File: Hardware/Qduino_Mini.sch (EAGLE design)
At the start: 39 parts, among them Q1 PFET, U1 ATMEGA32U4QFN, U2 MCP73831, U3 MAX17048, U4 TPS78233, Y1 16MHz

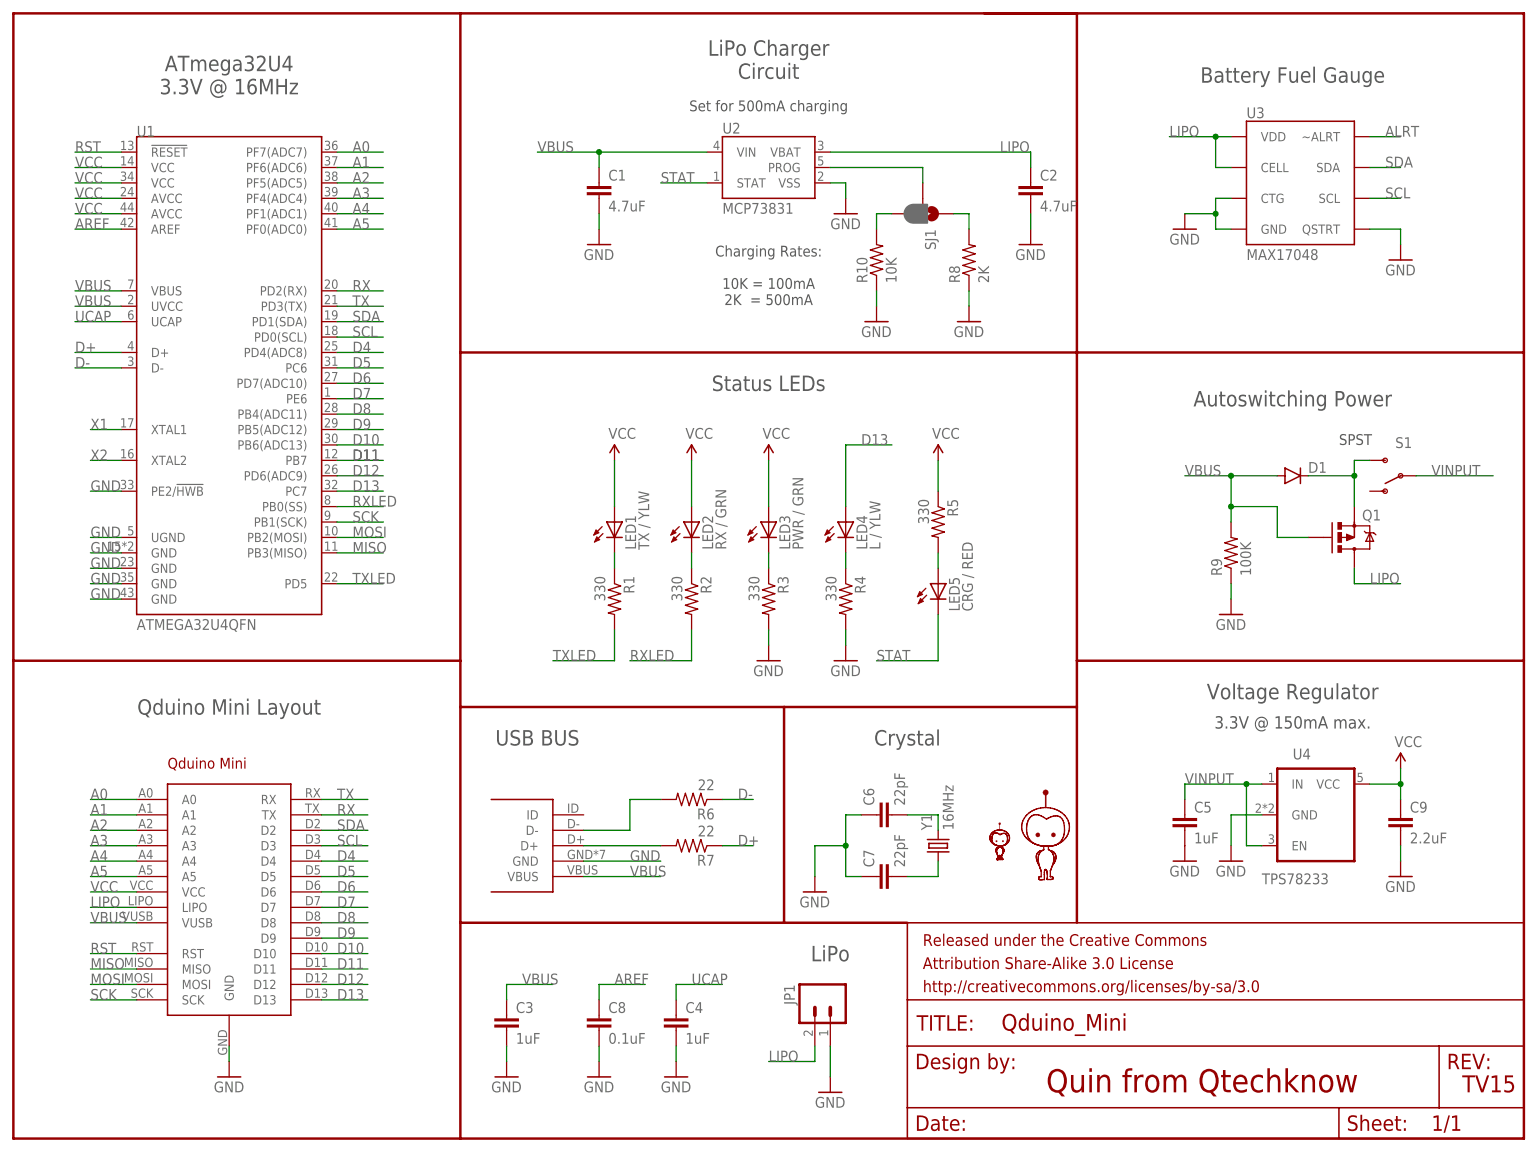
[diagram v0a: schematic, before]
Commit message: Converted simple things to SparkFun styles
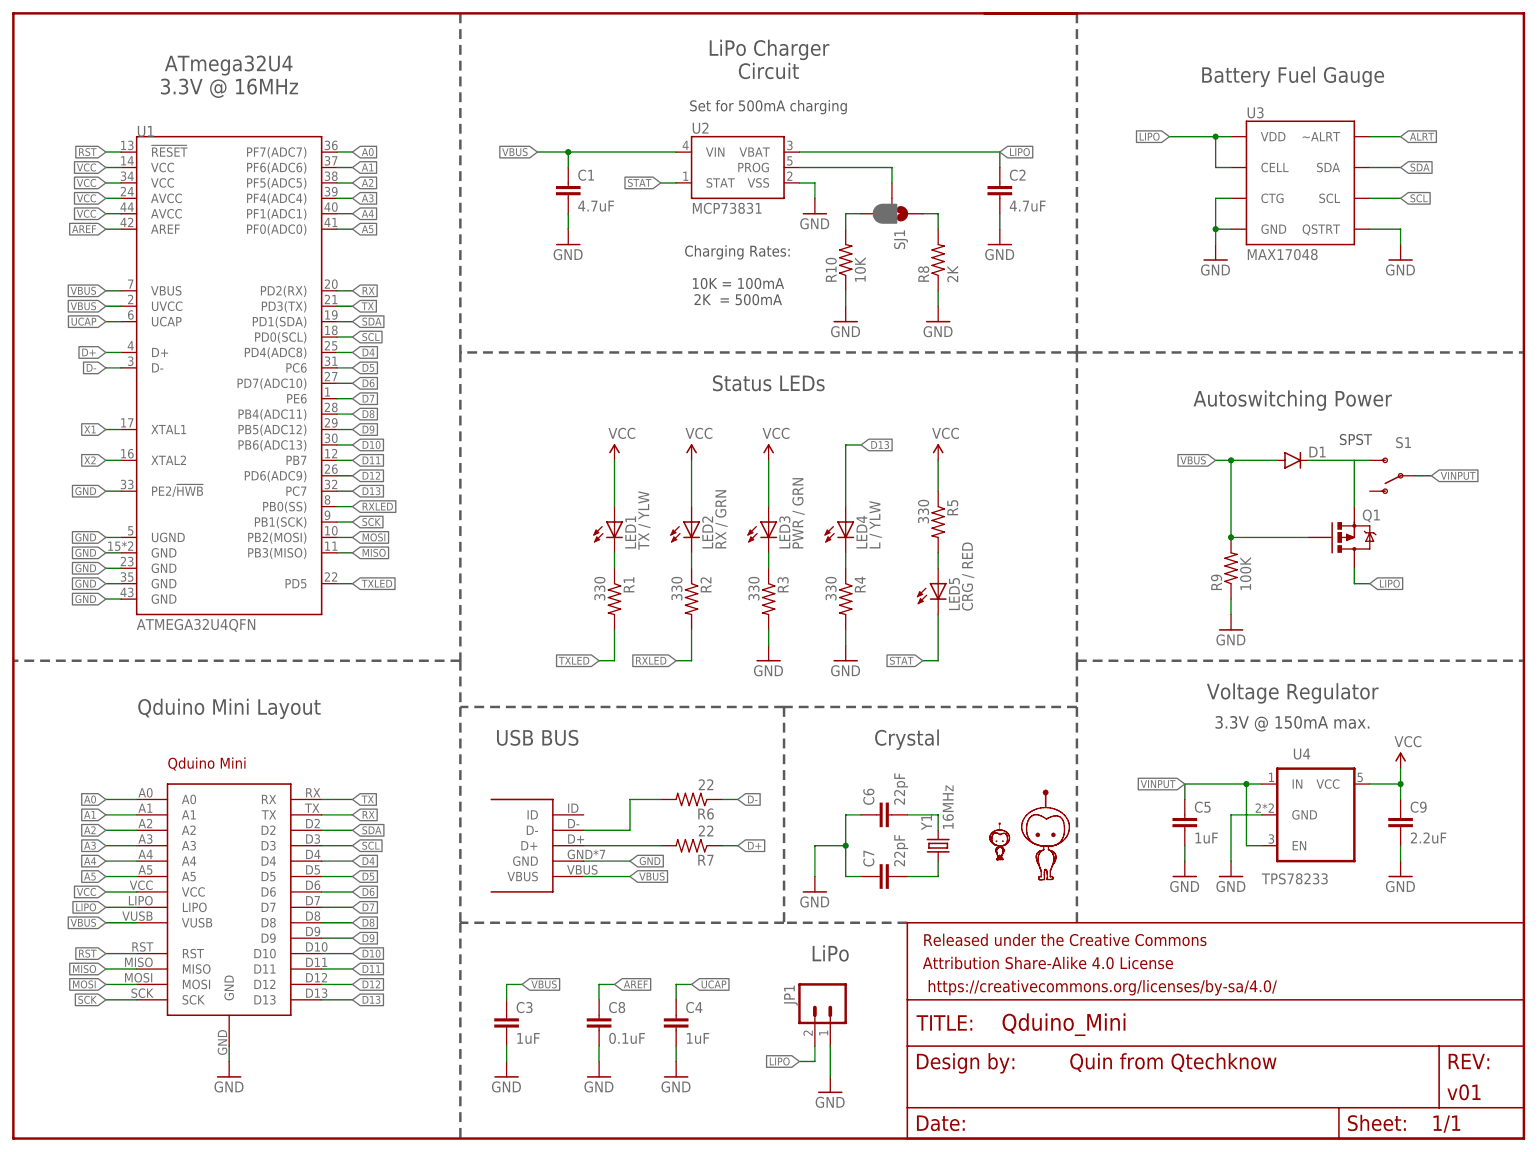
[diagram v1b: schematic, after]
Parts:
- FRAME2: value FRAME-LETTER -> (none); DESIGNER (none) -> Quin from Qtechknow
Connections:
- new net N$3: Q1.S
- net INMOSFET: no longer Q1.S
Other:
- note removed: "Quin from Qtechknow"
- note removed: "TV15"
- moved on the sheet: C1, C2, D1, R10, R8, R9, SJ1, U2

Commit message: Added pullup resistors, added alrt interrupt trace, added PROD_ID to each part, swapped out SFE already used parts, etc
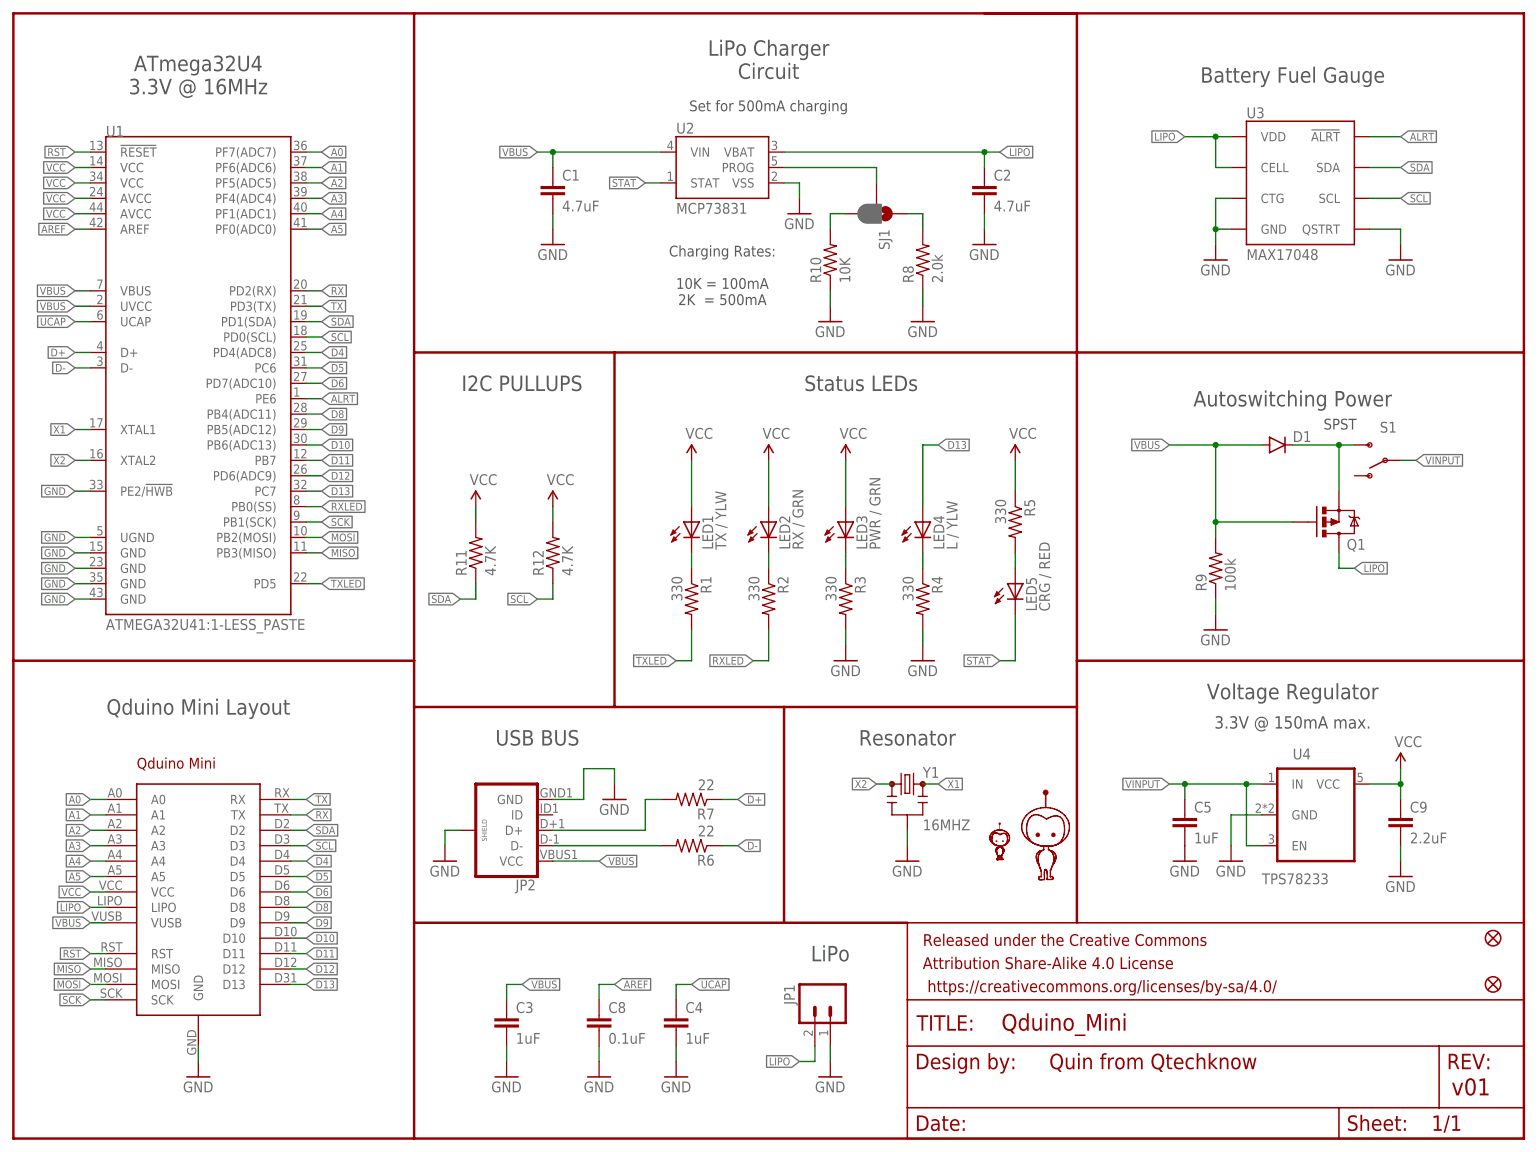
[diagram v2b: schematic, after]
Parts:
- removed C6, C7: 22pF, SparkFun-Passives:CAP0603-CAP
- removed JP3: QDUINOMINI, Qtechknow:QDUINOMINI
- added FID5, FID6: FIDUCIAL1X2, SparkFun-Aesthetics:FIDUCIAL1X2
- added R11, R12: 4.7K, SparkFun-Passives:RESISTOR0603-RES
- added U7: DNP, Qtechknow:QDUINOMINI
- C1, C2: PROD_ID (none) -> CAP-10300
- C3, C4, C5: PROD_ID (none) -> CAP-00868
- C8: device SparkFun-Passives:CAP0603-CAP -> SparkFun-Capacitors:0.1UF-25V(+80/-20%)(0603)
- C9: device SparkFun-Passives:CAP0603-CAP -> SparkFun-Capacitors:2.2UF-10V-20%(0603)
- FRAME2: DESIGNER Quin from Qtechknow -> (none)
- JP1: PROD_ID (none) -> CONN-11443
- JP2: value USB-MICROBQ -> USB_MICROB_PLUGCONN-11752; device SFE-Sockets:USB-MICROBQ -> SparkFun-Connectors:USB_MICROB_PLUGCONN-11752
- LED1, LED4: PROD_ID (none) -> DIO-09003
- LED2, LED3: PROD_ID (none) -> DIO-00821
- LED5: PROD_ID (none) -> DIO-00819
- Q1: device Pinoccio:MOSFET-PCHANNELSMD -> SparkFun-DiscreteSemi:MOSFET-PCHANNEL
- R1, R2, R3, R4, R5: PROD_ID (none) -> RES-00818
- R10: device SparkFun-Resistors:RESISTOR0603 -> SparkFun-Resistors:10KOHM-1/10W-1%(0603)0603
- R6, R7: PROD_ID (none) -> RES-08698
- R8: value 2K -> 2.0k; device SparkFun-Resistors:RESISTOR0603 -> SparkFun-Resistors:2.0KOHM1/10W5%(0603)
- R9: value 100K -> 100k; device SparkFun-Resistors:RESISTOR0603 -> SparkFun-Resistors:100KOHM-1/10W-1%(0603)
- U1: value ATMEGA32U4QFN -> ATMEGA32U41:1-LESS_PASTE; device SparkFun-DigitalIC:ATMEGA32U4QFN -> SparkFun-DigitalIC:ATMEGA32U41:1-LESS_PASTE; PROD_ID (none) -> IC-10828
- U2: PROD_ID (none) -> IC-09995
- U3: PROD_ID (none) -> IC-12551
- U4: PROD_ID (none) -> 12550
- Y1: value 16MHz -> 16MHZ; device SparkFun-FreqCtrl:CRYSTAL5X3 -> SparkFun-FreqCtrl:RESONATOR16MHZ
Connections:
- removed net D7: JP3.D7, U1.PE6
- removed net N$3: Q1.S
- net A0: now also U7.A0; no longer JP3.A0
- net A1: now also U7.A1; no longer JP3.A1
- net A2: now also U7.A2; no longer JP3.A2
- net A3: now also U7.A3; no longer JP3.A3
- net A4: now also U7.A4; no longer JP3.A4
- net A5: now also U7.A5; no longer JP3.A5
- net ALRT: now also U1.PE6, U3.!ALRT; no longer U3.~ALRT
- net D10: now also U7.D10; no longer JP3.D10
- net D11: now also U7.D11; no longer JP3.D11
- net D12: now also U7.D12; no longer JP3.D12
- net D13: now also U7.D13; no longer JP3.D13
- net D4: now also U7.D4; no longer JP3.D4
- net D5: now also U7.D5; no longer JP3.D5
- net D6: now also U7.D6; no longer JP3.D6
- net D8: now also U7.D8; no longer JP3.D8
- net D9: now also U7.D9; no longer JP3.D9
- net GND: now also JP2.SHIELD, U7.GND, Y1.2; no longer C6.1, C7.1, JP3.GND
- net INMOSFET: now also Q1.S
- net LIPO: now also U7.LIPO; no longer JP3.LIPO
- net MISO: now also U7.MISO; no longer JP3.MISO
- net MOSI: now also U7.MOSI; no longer JP3.MOSI
- net RST: now also U7.RST; no longer JP3.RST
- net RX: now also U7.TX; no longer JP3.TX
- net SCK: now also U7.SCK; no longer JP3.SCK
- net SCL: now also R12.1, U7.D3; no longer JP3.D3
- net SDA: now also R11.1, U7.D2; no longer JP3.D2
- net TX: now also U7.RX; no longer JP3.RX
- net VBUS: now also JP2.VCC, U7.VUSB; no longer JP2.VBUS, JP3.VUSB
- net VCC: now also R11.2, R12.2, U7.VCC; no longer JP3.VCC
- net X1: now also Y1.3; no longer C7.2, Y1.1
- net X2: now also Y1.1; no longer C6.2, Y1.2
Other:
- note added: "I2C PULLUPS"
- note added: "Resonator"
- note removed: "Crystal"
- moved on the sheet: C1, C2, D1, LED1, LED2, LED3, LED4, LED5, Q1, R1, R10, R2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

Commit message: Added missing prod_id for switch
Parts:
- S1: PROD_ID (none) -> SWCH-10651
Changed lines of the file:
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@@
 <attribute name="PROD_ID" value="CAP-00868"/>
 </part>
-<part name="S1" library="SparkFun-Electromechanical" deviceset="SWITCH-SPDT" device="-SMD-A"/>
+<part name="S1" library="SparkFun-Electromechanical" deviceset="SWITCH-SPDT" device="-SMD-A">
+<attribute name="PROD_ID" value="SWCH-10651"/>
+</part>
 <part name="U3" library="Pinoccio" deviceset="MAX17048" device="DFN8" value="MAX17048">
 <attribute name="PROD_ID" value="IC-12551"/>
@@
 <attribute name="PROD_ID" x="-5.08" y="-33.02" size="1.778" layer="96" display="off"/>
 </instance>
-<instance part="S1" gate="1" x="139.7" y="60.96" rot="R180"/>
+<instance part="S1" gate="1" x="139.7" y="60.96" rot="R180">
+<attribute name="PROD_ID" x="139.7" y="60.96" size="1.778" layer="96" rot="R180" display="off"/>
+</instance>
 <instance part="U3" gate="G$1" x="127" y="106.68">
 <attribute name="PROD_ID" x="127" y="106.68" size="1.27" layer="96" display="off"/>
